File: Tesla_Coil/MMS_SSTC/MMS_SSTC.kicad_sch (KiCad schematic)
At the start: 34 parts, among them J2 Screw_Terminal_01x02, Q1 IRFP460APBF, U1 NE555P, U2 UCC37322P, U3 LM7812_TO220

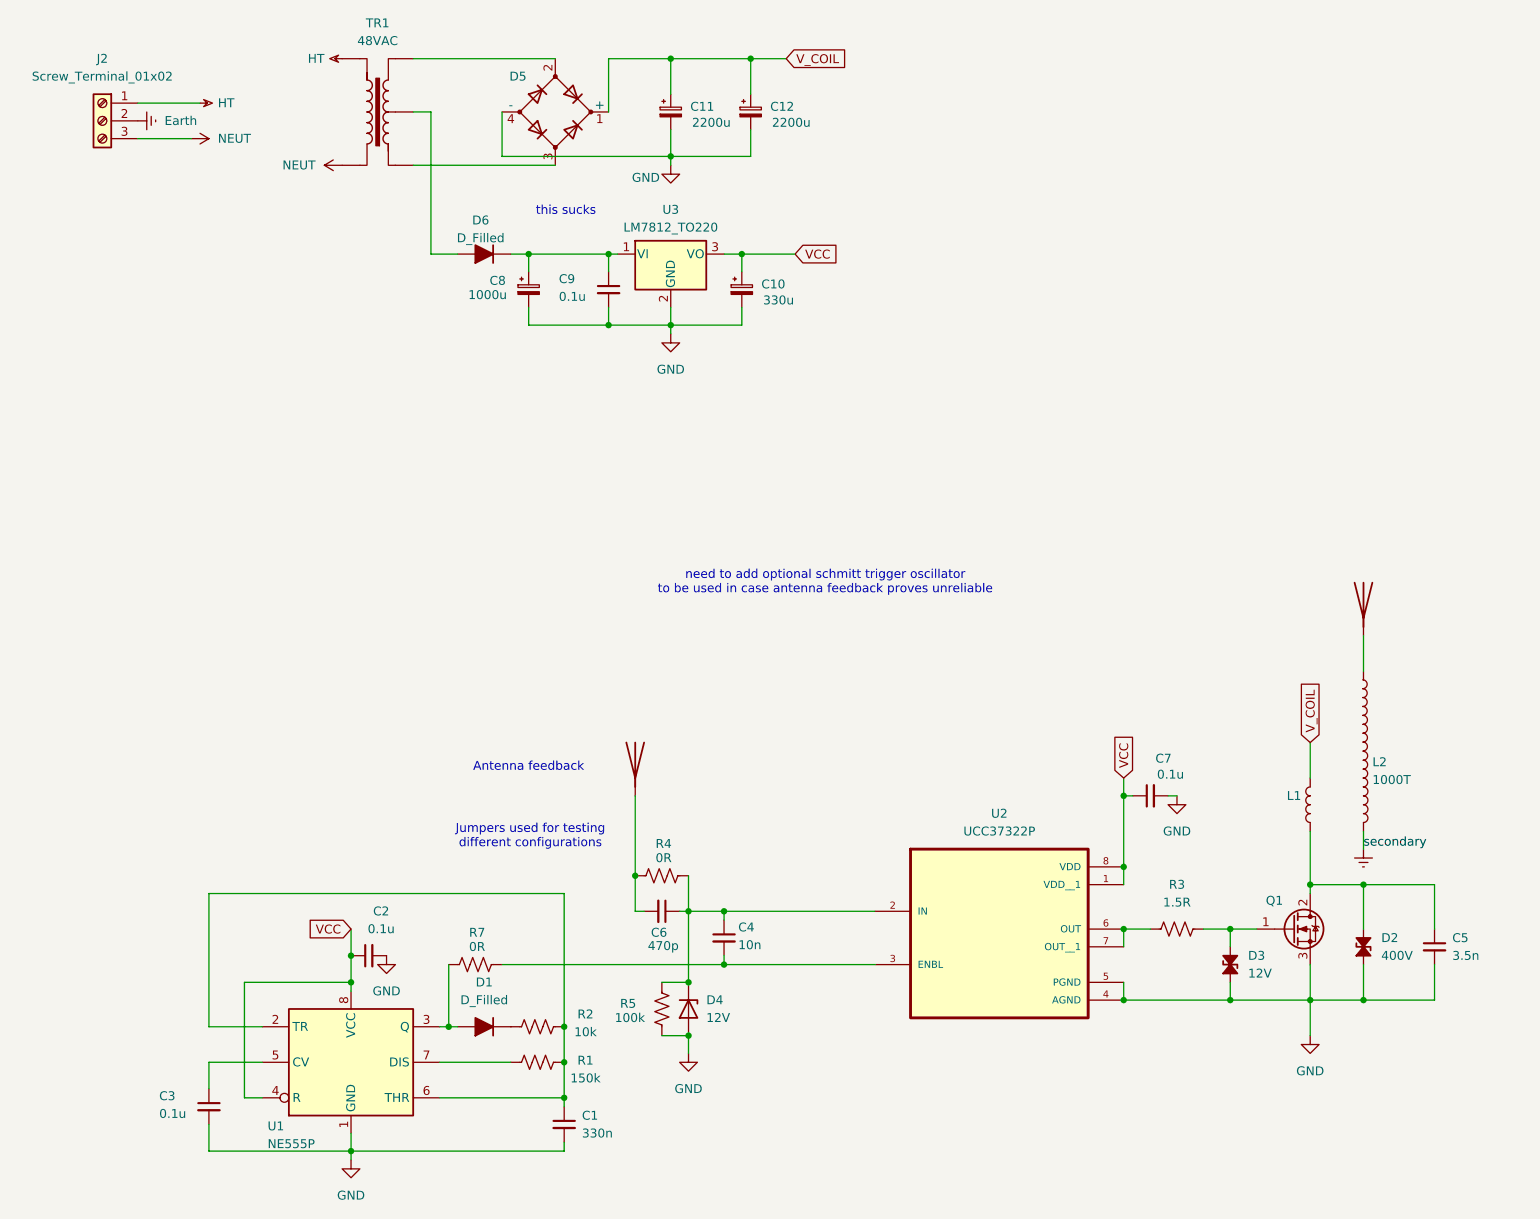
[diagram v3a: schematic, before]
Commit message: Update supporting files for schematic oops
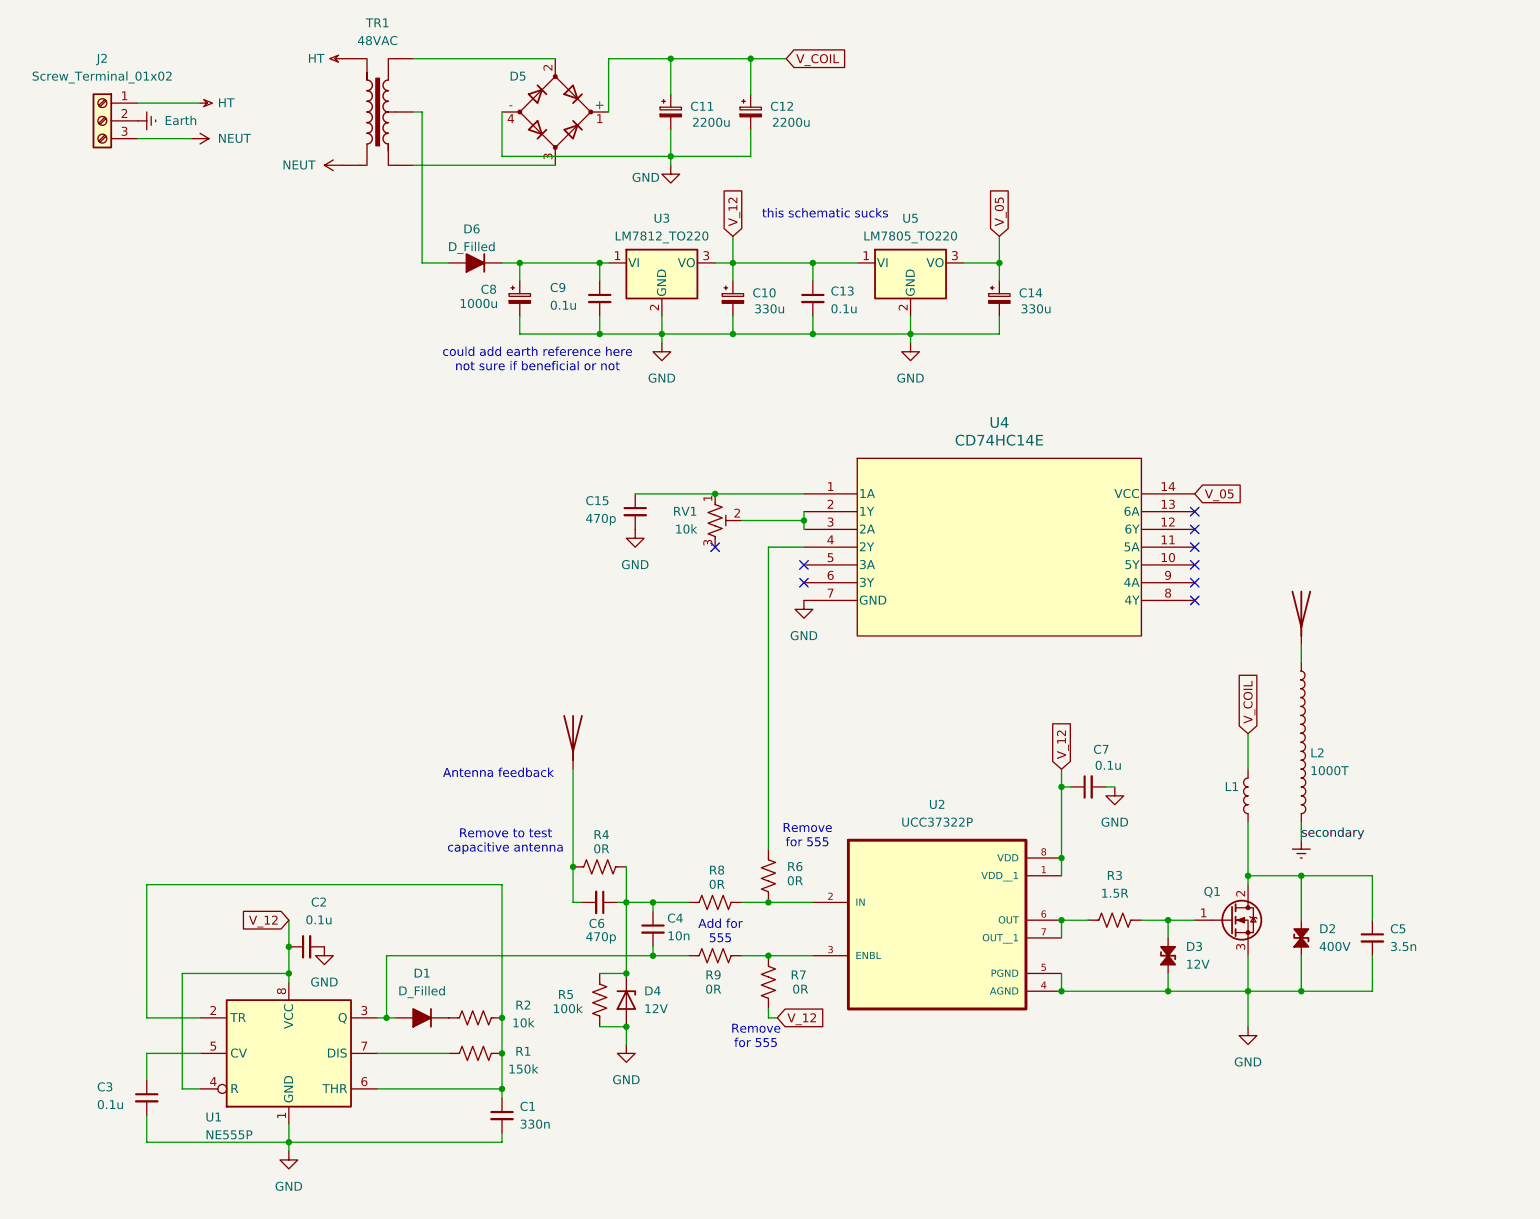
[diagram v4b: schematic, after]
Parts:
- added C13: 0.1u, symbol Device:C_Small
- added C14: 330u, symbol Device:C_Polarized_Small
- added C15: 470p, symbol Device:C_Small
- added R6, R8, R9: 0R, symbol Device:R_US
- added RV1: 10k, symbol Device:R_Potentiometer_Trim_US
- added U4: CD74HC14E, N14, symbol locals:CD74HC14E
- added U5: LM7805_TO220, Package_TO_SOT_THT:TO-220-3_Vertical, symbol Regulator_Linear:LM7805_TO220
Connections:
- net GND: now also C13.2, C14.2, C15.2, U4.7 (GND), U5.2 (GND)
- net at C4.1, C6.1, D4.1 (K)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: now also R8.2; no longer U2.2 (IN)
- net at R7.1, U2.3 (ENBL): now also R9.1; no longer C4.2
- net at D1.2 (A), U1.3 (Q): now also C4.2, R9.2; no longer R7.2
- net VCC renamed V_12
- net V_12: now also R7.2, C13.1, U5.1 (VI)
- new net: C15.1, RV1.1, U4.1 (1A)
- new net: R6.1, U4.4 (2Y)
- new net: R6.2, R8.1, U2.2 (IN)
- new net: RV1.2, U4.2 (1Y), U4.3 (2A)
- new net V_05: C14.1, U4.14 (VCC), U5.3 (VO)
- no-connect marks 0 -> 9
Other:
- note added: "Add for 555"
- note added: "Remove for 555"
- note added: "Remove to test capacitive antenna"
- note added: "could add earth reference here not sure if beneficial or not"
- note added: "this schematic sucks"
- note removed: "Jumpers used for testing different configurations"
- note removed: "need to add optional schmitt trigger oscillator to be used in case antenna feedback proves unreliable"
- note removed: "this sucks"
- moved on the sheet: C1, C10, C2, C3, C4, C5, C6, C7, C8, C9, D1, D2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

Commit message: Minor tweaks to schematic, needs finished and all details added
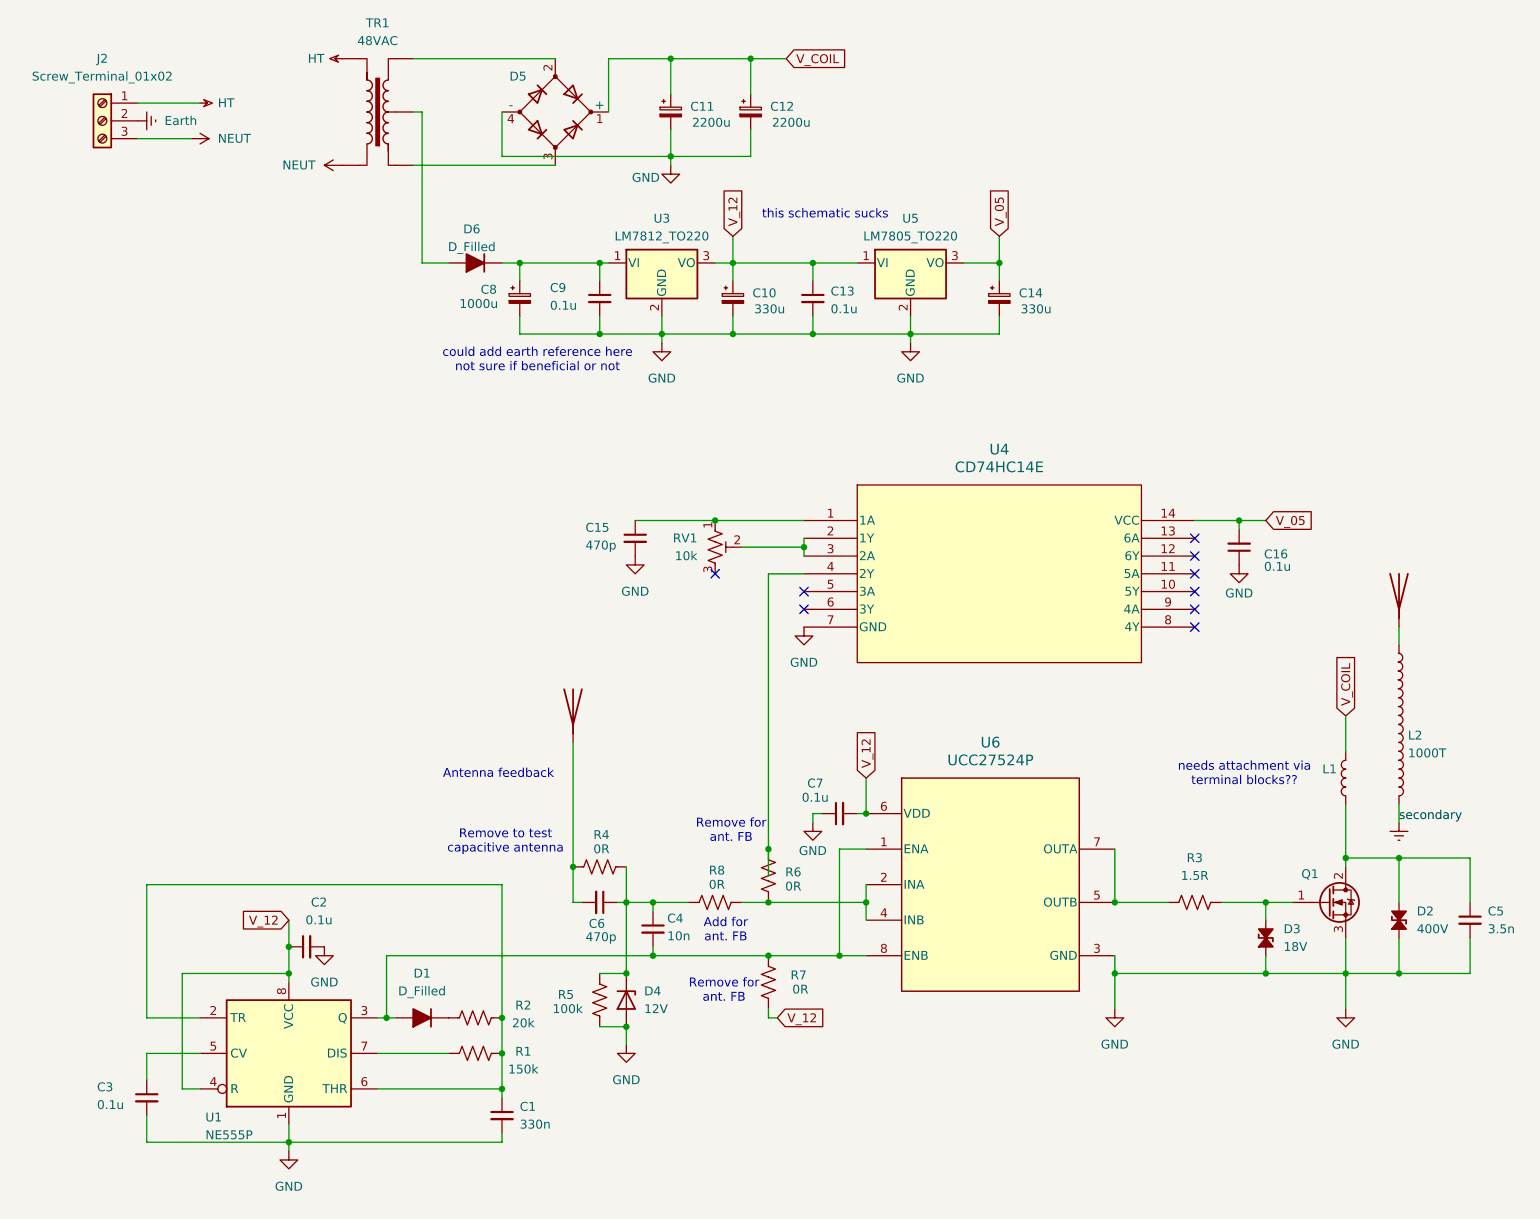
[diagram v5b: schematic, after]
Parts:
- removed R9: 0R, symbol Device:R_US
- removed U2: UCC37322P, UCC37322P:DIP794W45P254L959H508Q8, symbol locals:UCC37322P
- added C16: 0.1u, symbol Device:C_Small
- added U6: UCC27524P, P0008A, symbol locals:UCC27524P
- C13, C2, C3, C7, C9: DKPN (none) -> 399-4264-ND
- D2: DKPN (none) -> 1.5KE400CALFCT-ND
- D3: value 12V -> 18V; DKPN (none) -> 497-11374-1-ND
- D4: DKPN (none) -> 1N4742AFS-ND
- D5: value D_Bridge_+AA- -> GBU810; DKPN (none) -> GBU810DI-ND
- R2: value 10k -> 20k
- U1: DKPN (none) -> 296-NE555P-ND
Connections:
- net GND: now also C7.1, C16.1, U6.3 (GND); no longer C7.2
- net V_05: now also C16.2
- net V_12: now also C7.2, U6.6 (VDD); no longer C7.1
- net at C4.2, D1.2 (A), U1.3 (Q): now also R7.1, U6.1 (ENA), U6.8 (ENB)
- net at R6.2, R8.1: now also U6.2 (INA), U6.4 (INB)
- net at R3.1: now also U6.5 (OUTB), U6.7 (OUTA)
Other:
- note added: "Add for ant. FB"
- note added: "Remove for ant. FB"
- note added: "needs attachment via terminal blocks??"
- note removed: "Add for 555"
- note removed: "Remove for 555"
- moved on the sheet: C15, C5, D2, D3, L1, L2, Q1, R3, RV1, U4
